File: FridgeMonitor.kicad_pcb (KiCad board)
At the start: 2 copper layers, 78 x 62 mm, 26 parts, among them J1 Conn_01x03, J2 Conn_01x03, J3 Conn_01x03, J4 Conn_01x03, J6 Conn_02x04_Odd_Even, J7 USB_B_Micro, U1 ESP-01v090, U2 LM2594M-3.3

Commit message: Backup
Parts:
- added JP1: SolderJumper_3_Bridged12, Jumper:SolderJumper-3_P1.3mm_Open_Pad1.0x1.5mm, F.Cu at (96.5, 80.0)
- added JP2: SolderJumper_3_Bridged12, Jumper:SolderJumper-3_P1.3mm_Open_Pad1.0x1.5mm, F.Cu at (77.5, 80.0)
- added JP3: SolderJumper_3_Bridged12, Jumper:SolderJumper-3_P1.3mm_Open_Pad1.0x1.5mm, F.Cu at (61.0, 80.0)
- added JP4: SolderJumper_3_Bridged12, Jumper:SolderJumper-3_P1.3mm_Open_Pad1.0x1.5mm, F.Cu at (53.3, 80.0)
- added R5: 0R, Resistor_SMD:R_0805_2012Metric_Pad1.20x1.40mm_HandSolder, F.Cu at (88.0, 51.5)
- added R6: 100k, Resistor_SMD:R_0805_2012Metric_Pad1.20x1.40mm_HandSolder, F.Cu at (88.0, 54.4)
- added REF**: MountingHole_3.2mm_M3, MountingHole:MountingHole_3.2mm_M3, F.Cu at (104.5, 86.0)
- added REF**: MountingHole_3.2mm_M3, MountingHole:MountingHole_3.2mm_M3, F.Cu at (69.0, 36.0)
- added REF**: MountingHole_3.2mm_M3, MountingHole:MountingHole_3.2mm_M3, F.Cu at (33.5, 36.0)
- added REF**: MountingHole_3.2mm_M3, MountingHole:MountingHole_3.2mm_M3, F.Cu at (33.5, 86.0)
- added REF**: MountingHole_3.2mm_M3, MountingHole:MountingHole_3.2mm_M3, F.Cu at (104.5, 36.0)
- moved D3 4.63 mm to (46.5, 39.5)
- moved R2 4.06 mm to (54.6, 74.9)
- moved R3 4.01 mm to (59.7, 75.0)
- moved C9 3.67 mm to (41.7, 39.5)
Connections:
- C1 pad 1: +3V3 -> Net-(J1-Pin_3)
- C2 pad 1: +3V3 -> Net-(J2-Pin_3)
- C3 pad 1: +3V3 -> Net-(J3-Pin_3)
- C4 pad 1: +3V3 -> Net-(J4-Pin_3)
- C5 pad 1: +3V3 -> Net-(J1-Pin_3)
- C6 pad 1: +3V3 -> Net-(J2-Pin_3)
- C7 pad 1: +3V3 -> Net-(J3-Pin_3)
- C8 pad 1: +3V3 -> Net-(J4-Pin_3)
- J1 pad 3: +3V3 -> Net-(J1-Pin_3)
- J2 pad 3: +3V3 -> Net-(J2-Pin_3)
- J3 pad 3: +3V3 -> Net-(J3-Pin_3)
- J4 pad 3: +3V3 -> Net-(J4-Pin_3)
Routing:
- net +3V3: track 163.6 -> 125.2 mm, vias 1 -> 4
- net Net-(J2-Pin_3): track 0.00 -> 20.9 mm
- net Net-(J4-Pin_3): track 0.00 -> 18.7 mm
- net Net-(J1-Pin_3): track 0.00 -> 16.4 mm
- net Net-(J3-Pin_3): track 0.00 -> 16.3 mm
- net /1-Wire: track 70.0 -> 83.6 mm
- net Net-(D3-K): track 7.97 -> 12.8 mm
- net Net-(J7-VBUS): track 20.0 -> 16.4 mm
- net Net-(J6-Pin_6): track 37.4 -> 34.1 mm

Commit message: For the moment all routed, except GND
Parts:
- added Q1: SI2301, Package_TO_SOT_SMD:TSOT-23, F.Cu at (60.7, 69.7)
- moved R6 35.1 mm to (56.4, 69.6), turned to 90 degrees
- moved R5 33.2 mm to (58.2, 66.0), turned to 180 degrees
- moved R1 3.95 mm to (41.9, 80.3), turned to -90 degrees
- moved C4 1.27 mm to (48.0, 82.5)
- moved J6 0.51 mm to (34.3, 77.0)
- moved C8 0.09 mm to (47.1, 76.2)
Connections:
- JP1 pad 3: unconnected-(JP1-B-Pad3) -> /V_sensors
- JP2 pad 3: unconnected-(JP2-B-Pad3) -> /V_sensors
- JP3 pad 3: unconnected-(JP3-B-Pad3) -> /V_sensors
- JP4 pad 3: unconnected-(JP4-B-Pad3) -> /V_sensors
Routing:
- net /V_sensors: track 0.00 -> 59.8 mm, vias 0 -> 3
- net Net-(J6-Pin_4): track 12.0 -> 47.8 mm
- net +3V3: track 125.2 -> 143.5 mm, vias 4 -> 5
- net /1-Wire: track 83.6 -> 96.4 mm
- net Net-(Q1-G): track 0.00 -> 5.87 mm
- net Net-(J4-Pin_3): track 18.7 -> 20.6 mm

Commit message: backup
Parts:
- removed the REF** at (69.0, 36.0)
- added ? (x2): , , F.Cu at (91.9, 46.5)
- added ?: , , F.Cu at (89.4, 51.6)
- added ?: , , F.Cu at (48.8, 51.6)
- added ?: , , F.Cu at (69.1, 43.9)
- added ?: , , F.Cu at (86.9, 46.5)
- added ?: , , F.Cu at (79.2, 46.5)
- added ?: , , F.Cu at (94.5, 43.9)
- added ?: , , F.Cu at (81.8, 46.5)
- added ?: , , F.Cu at (102.1, 46.5)
- added ?: , , F.Cu at (79.2, 51.6)
- added ?: , , F.Cu at (74.2, 43.9)
- added ?: , , F.Cu at (91.9, 43.9)
- added ?: , , F.Cu at (69.1, 46.5)
- added ?: , , F.Cu at (71.6, 51.6)
- added ?: , , F.Cu at (86.9, 51.6)
- added ?: , , F.Cu at (74.2, 46.5)
- added ?: , , F.Cu at (61.5, 51.6)
- added ?: , , F.Cu at (99.6, 43.9)
- added ?: , , F.Cu at (97.0, 51.6)
- added ?: , , F.Cu at (94.5, 51.6)
- added ?: , , F.Cu at (76.7, 51.6)
- added ?: , , F.Cu at (58.9, 51.6)
- added ?: , , F.Cu at (53.8, 51.6)
- added ?: , , F.Cu at (66.5, 51.6)
- added ?: , , F.Cu at (84.3, 43.9)
- added ?: , , F.Cu at (91.9, 51.6)
- added ?: , , F.Cu at (71.6, 43.9)
- added ?: , , F.Cu at (76.7, 46.5)
- added ?: , , F.Cu at (89.4, 43.9)
- added ?: , , F.Cu at (69.1, 51.6)
- added ?: , , F.Cu at (51.3, 51.6)
- added ?: , , F.Cu at (81.8, 51.6)
- added ?: , , F.Cu at (97.0, 43.9)
- added ?: , , F.Cu at (99.6, 46.5)
- added ?: , , F.Cu at (84.3, 46.5)
- added ?: , , F.Cu at (71.6, 46.5)
- added ?: , , F.Cu at (94.5, 46.5)
- added ?: , , F.Cu at (64.0, 51.6)
- added ?: , , F.Cu at (74.2, 51.6)
- added ?: , , F.Cu at (97.0, 46.5)
- added ?: , , F.Cu at (102.1, 43.9)
- added ?: , , F.Cu at (84.3, 51.6)
- added ?: , , F.Cu at (56.4, 51.6)
- added ?: , , F.Cu at (86.9, 43.9)
- added ?: , , F.Cu at (89.4, 46.5)
- added ?: , , F.Cu at (81.8, 43.9)
- added ?: , , F.Cu at (104.6, 43.9)
- added A1: RaspberryPi_Pico, OwnFootprints:EVB_PICO, F.Cu at (53.8, 66.8)
- added C13: C_Polarized, Capacitor_THT:CP_Radial_D6.3mm_P2.50mm, F.Cu at (78.9, 41.2)
- added C14: C, Capacitor_SMD:C_0805_2012Metric_Pad1.18x1.45mm_HandSolder, F.Cu at (82.9, 38.8)
- added C15: C_Polarized, Capacitor_THT:CP_Radial_D6.3mm_P2.50mm, F.Cu at (64.5, 33.8)
- added C16: C, Capacitor_SMD:C_0805_2012Metric_Pad1.18x1.45mm_HandSolder, F.Cu at (66.3, 38.6)
- added J10: Conn_01x02_Pin, Connector_PinSocket_2.54mm:PinSocket_1x02_P2.54mm_Vertical, F.Cu at (71.6, 41.4)
- added J11: Conn_01x03, Connector_Phoenix_MC_HighVoltage:PhoenixContact_MC_1,5_3-G-5.08_1x03_P5.08mm_Horizontal, F.Cu at (80.2, 35.2)
- added J5: Conn_01x03, Connector_Phoenix_MC_HighVoltage:PhoenixContact_MC_1,5_3-G-5.08_1x03_P5.08mm_Horizontal, F.Cu at (97.0, 35.3)
- added J8: Conn_01x02_Pin, Connector_PinSocket_2.54mm:PinSocket_1x02_P2.54mm_Vertical, F.Cu at (89.4, 41.4)
- added J9: Conn_01x02_Pin, Connector_PinSocket_2.54mm:PinSocket_1x02_P2.54mm_Vertical, F.Cu at (32.2, 41.5)
- moved Q1 27.3 mm to (37.7, 55.2), turned to 90 degrees
- moved R5 25.5 mm to (34.0, 57.8), turned to -90 degrees
- moved R6 21.3 mm to (37.6, 59.5), turned to 180 degrees
- moved C12 19.3 mm to (62.0, 44.7), turned to 90 degrees
- moved L1 15.0 mm to (53.5, 33.5), turned to -90 degrees
- moved D3 5.52 mm to (46.0, 45.0)
- moved R4 4.02 mm to (41.0, 52.0), turned to 180 degrees
- moved C10 3.79 mm to (45.0, 69.0), turned to -90 degrees
- moved C11 1.69 mm to (49.5, 69.0), turned to -90 degrees
- moved C8 1.33 mm to (46.8, 77.5)
- moved JP4 0.69 mm to (54.0, 80.0)
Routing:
- net +3V3: track 143.5 -> 175.3 mm, vias 5 -> 6
- net /V_sensors: track 59.8 -> 91.4 mm, vias 3 -> 4
- net Net-(J6-Pin_4): track 47.8 -> 18.3 mm
- net Net-(J5-Pin_3): track 0.00 -> 17.1 mm
- net Net-(D3-K): track 12.8 -> 22.4 mm
- net Net-(J10-Pin_2): track 0.00 -> 8.35 mm
- net Net-(J7-VBUS): track 16.4 -> 24.1 mm
- net Net-(J10-Pin_1): track 0.00 -> 7.66 mm
- net Net-(J5-Pin_2): track 0.00 -> 7.15 mm
- net Net-(J4-Pin_3): track 20.6 -> 19.7 mm
- net Net-(U2-~{ON}/OFF): track 2.66 -> 1.98 mm
- net Net-(J6-Pin_6): track 34.1 -> 33.5 mm

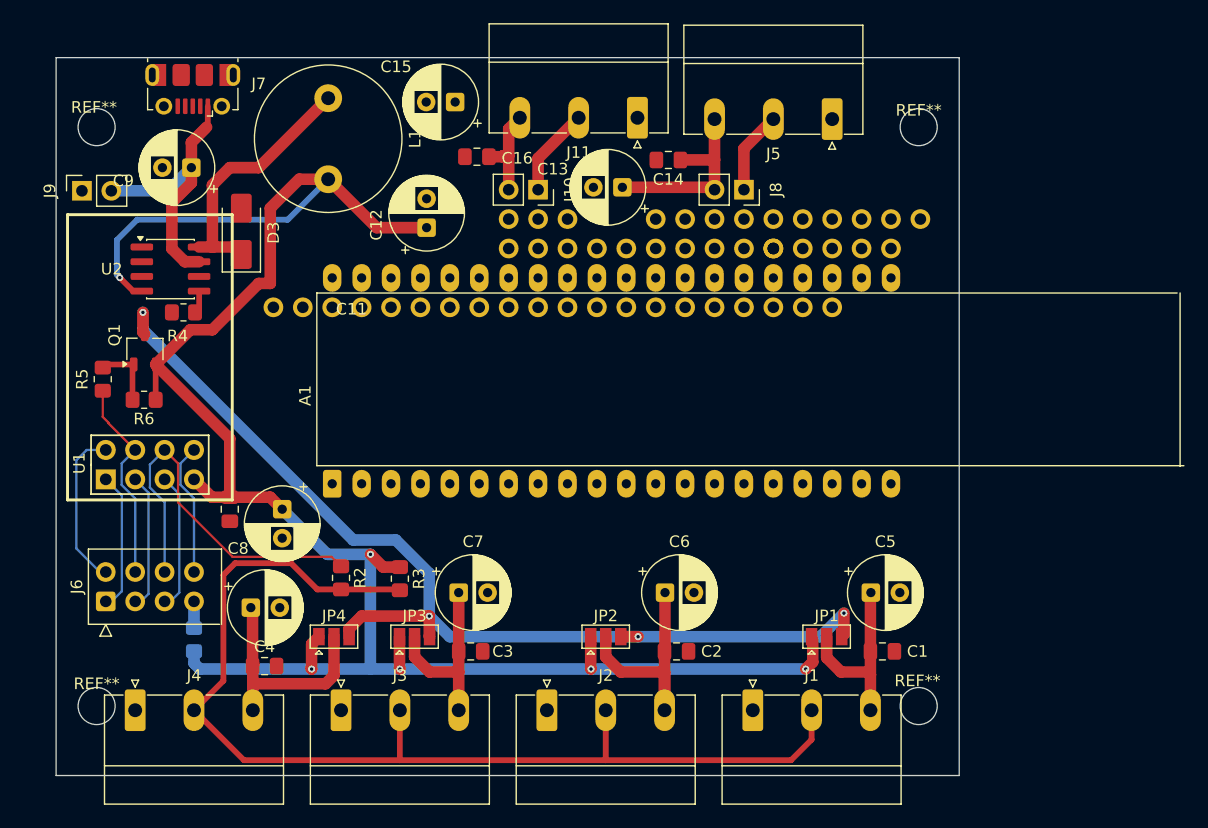
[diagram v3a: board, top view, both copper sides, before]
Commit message: all routed, except GND
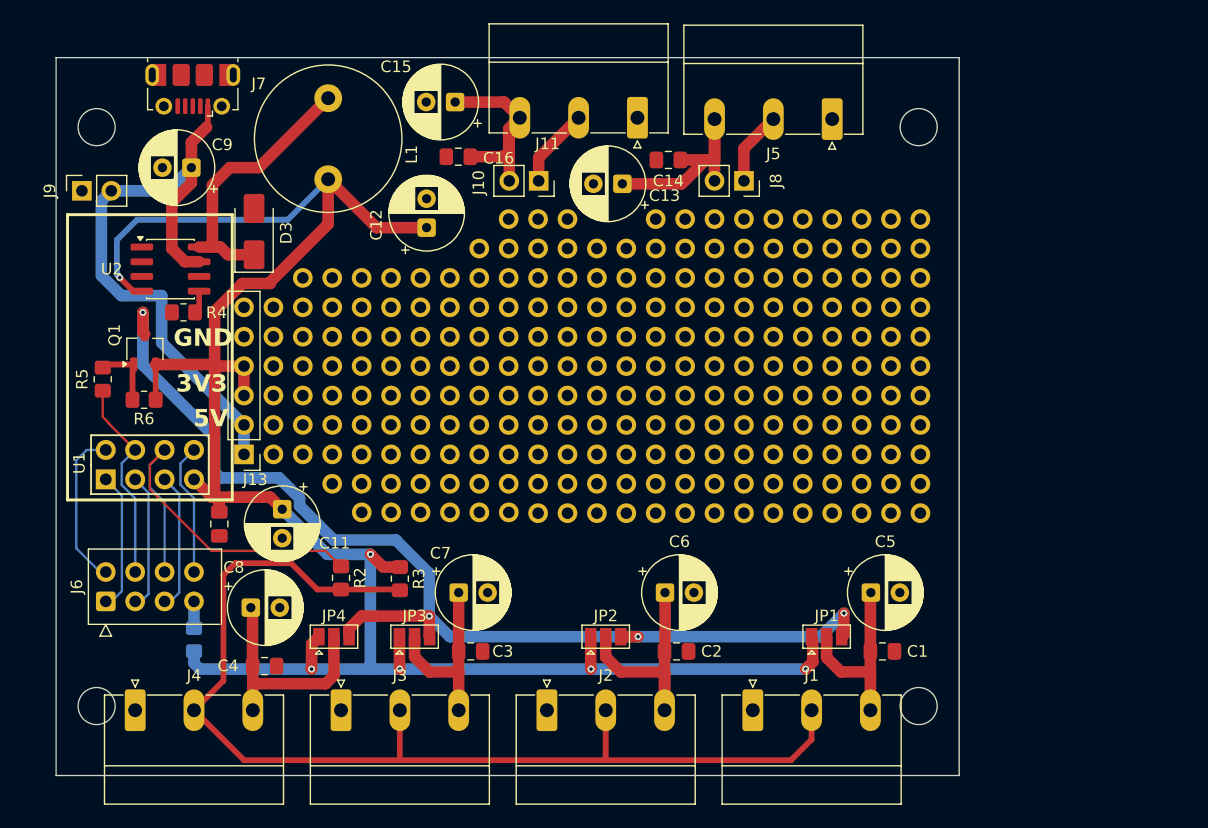
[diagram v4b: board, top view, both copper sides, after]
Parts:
- removed the ? at (91.9, 46.5)
- removed A1: RaspberryPi_Pico, OwnFootprints:EVB_PICO
- added ?: , , F.Cu at (104.6, 59.2)
- added ?: , , F.Cu at (61.5, 69.3)
- added ?: , , F.Cu at (81.8, 54.1)
- added ?: , , F.Cu at (86.9, 61.7)
- added ?: , , F.Cu at (89.4, 66.8)
- added ?: , , F.Cu at (64.0, 54.1)
- added ?: , , F.Cu at (91.9, 66.8)
- added ?: , , F.Cu at (61.5, 54.1)
- added ?: , , F.Cu at (76.7, 69.3)
- added ?: , , F.Cu at (84.3, 64.3)
- added ?: , , F.Cu at (69.1, 61.7)
- added ?: , , F.Cu at (74.2, 61.7)
- added ?: , , F.Cu at (91.9, 49.0)
- added ?: , , F.Cu at (69.1, 64.3)
- added ?: , , F.Cu at (102.1, 64.3)
- added ?: , , F.Cu at (51.3, 54.1)
- added ?: , , F.Cu at (89.4, 61.7)
- added ?: , , F.Cu at (89.4, 54.1)
- added ?: , , F.Cu at (79.2, 49.0)
- added ?: , , F.Cu at (76.7, 56.6)
- added ?: , , F.Cu at (53.8, 64.3)
- added ?: , , F.Cu at (64.0, 61.7)
- added ?: , , F.Cu at (84.3, 54.1)
- added ?: , , F.Cu at (89.4, 49.0)
- added ?: , , F.Cu at (97.0, 64.3)
- added ?: , , F.Cu at (58.9, 49.0)
- added ?: , , F.Cu at (102.1, 49.0)
- added ?: , , F.Cu at (97.0, 61.7)
- added ?: , , F.Cu at (99.6, 61.7)
- added ?: , , F.Cu at (94.5, 59.2)
- added ?: , , F.Cu at (56.4, 61.7)
- added ?: , , F.Cu at (58.9, 64.3)
- added ?: , , F.Cu at (91.9, 59.2)
- added ?: , , F.Cu at (69.1, 49.0)
- added ?: , , F.Cu at (51.3, 59.2)
- added ?: , , F.Cu at (102.1, 66.8)
- added ?: , , F.Cu at (74.2, 54.1)
- added ?: , , F.Cu at (58.9, 69.3)
- added ?: , , F.Cu at (53.8, 56.6)
- added ?: , , F.Cu at (66.5, 54.1)
- added ?: , , F.Cu at (94.5, 54.1)
- added ?: , , F.Cu at (99.6, 66.8)
- added ?: , , F.Cu at (74.2, 66.8)
- added ?: , , F.Cu at (84.3, 59.2)
- added ?: , , F.Cu at (97.0, 69.3)
- added ?: , , F.Cu at (58.9, 54.1)
- added ?: , , F.Cu at (71.6, 59.2)
- added ?: , , F.Cu at (104.6, 51.6)
- added ?: , , F.Cu at (76.7, 49.0)
- added ?: , , F.Cu at (56.4, 54.1)
- added ?: , , F.Cu at (89.4, 59.2)
- added ?: , , F.Cu at (69.1, 59.2)
- added ?: , , F.Cu at (76.7, 66.8)
- added ?: , , F.Cu at (79.2, 54.1)
- added ?: , , F.Cu at (61.5, 56.6)
- added ?: , , F.Cu at (74.2, 69.3)
- added ?: , , F.Cu at (99.6, 49.0)
- added ?: , , F.Cu at (102.1, 56.6)
- added ?: , , F.Cu at (56.4, 49.0)
- added ?: , , F.Cu at (64.0, 66.8)
- added ?: , , F.Cu at (51.3, 56.6)
- added ?: , , F.Cu at (86.9, 64.3)
- added ?: , , F.Cu at (74.2, 59.2)
- added ?: , , F.Cu at (53.8, 54.1)
- added ?: , , F.Cu at (64.0, 56.6)
- added ?: , , F.Cu at (71.6, 49.0)
- added ?: , , F.Cu at (56.4, 56.6)
- added ?: , , F.Cu at (99.6, 54.1)
- added ?: , , F.Cu at (48.8, 64.3)
- added ?: , , F.Cu at (94.5, 69.3)
- added ?: , , F.Cu at (61.5, 64.3)
- added ?: , , F.Cu at (58.9, 59.2)
- added ?: , , F.Cu at (97.0, 59.2)
- added ?: , , F.Cu at (71.6, 56.6)
- added ?: , , F.Cu at (89.4, 69.3)
- added ?: , , F.Cu at (66.5, 56.6)
- added ?: , , F.Cu at (81.8, 66.8)
- added ?: , , F.Cu at (71.6, 61.7)
- added ?: , , F.Cu at (86.9, 54.1)
- added ?: , , F.Cu at (53.8, 66.8)
- added ?: , , F.Cu at (104.6, 66.8)
- added ?: , , F.Cu at (94.5, 61.7)
- added ?: , , F.Cu at (102.1, 69.3)
- added ?: , , F.Cu at (104.6, 61.7)
- added ?: , , F.Cu at (51.3, 64.3)
- added ?: , , F.Cu at (97.0, 54.1)
- added ?: , , F.Cu at (97.0, 49.0)
- added ?: , , F.Cu at (66.5, 66.8)
- added ?: , , F.Cu at (56.4, 59.2)
- added ?: , , F.Cu at (91.9, 69.3)
- added ?: , , F.Cu at (79.2, 64.3)
- added ?: , , F.Cu at (86.9, 66.8)
- added ?: , , F.Cu at (53.8, 61.7)
- added ?: , , F.Cu at (61.5, 66.8)
- added ?: , , F.Cu at (71.6, 66.8)
- added ?: , , F.Cu at (94.5, 49.0)
- added ?: , , F.Cu at (99.6, 69.3)
- added ?: , , F.Cu at (104.6, 46.5)
- added ?: , , F.Cu at (102.1, 61.7)
- added ?: , , F.Cu at (79.2, 69.3)
- added ?: , , F.Cu at (71.6, 54.1)
- added ?: , , F.Cu at (91.9, 54.1)
- added ?: , , F.Cu at (86.9, 49.0)
- added ?: , , F.Cu at (66.5, 49.0)
- added ?: , , F.Cu at (94.5, 64.3)
- added ?: , , F.Cu at (51.3, 61.7)
- added ?: , , F.Cu at (48.8, 59.2)
- added ?: , , F.Cu at (104.6, 56.6)
- added ?: , , F.Cu at (66.6, 69.3)
- added ?: , , F.Cu at (84.3, 49.0)
- added ?: , , F.Cu at (94.5, 66.8)
- added ?: , , F.Cu at (58.9, 56.6)
- added ?: , , F.Cu at (99.6, 51.6)
- added ?: , , F.Cu at (97.0, 56.6)
- added ?: , , F.Cu at (64.0, 59.2)
- added ?: , , F.Cu at (104.6, 54.1)
- added ?: , , F.Cu at (48.8, 61.7)
- added ?: , , F.Cu at (58.9, 61.7)
- added ?: , , F.Cu at (56.4, 69.3)
- added ?: , , F.Cu at (79.2, 61.7)
- added ?: , , F.Cu at (56.4, 64.3)
- added ?: , , F.Cu at (51.3, 49.0)
- added ?: , , F.Cu at (81.8, 64.3)
- added ?: , , F.Cu at (71.6, 64.3)
- added ?: , , F.Cu at (76.7, 64.3)
- added ?: , , F.Cu at (76.7, 61.7)
- added ?: , , F.Cu at (74.2, 56.6)
- added ?: , , F.Cu at (71.6, 69.3)
- added ?: , , F.Cu at (102.1, 59.2)
- added ?: , , F.Cu at (81.8, 69.3)
- added ?: , , F.Cu at (104.6, 49.0)
- added ?: , , F.Cu at (84.3, 61.7)
- added ?: , , F.Cu at (86.9, 56.6)
- added ?: , , F.Cu at (66.5, 59.2)
- added ?: , , F.Cu at (102.1, 54.1)
- added ?: , , F.Cu at (58.9, 66.8)
- added ?: , , F.Cu at (53.8, 49.0)
- added ?: , , F.Cu at (91.9, 64.3)
- added ?: , , F.Cu at (74.2, 49.0)
- added ?: , , F.Cu at (64.0, 49.0)
- added ?: , , F.Cu at (81.8, 59.2)
- added ?: , , F.Cu at (64.0, 69.3)
- added ?: , , F.Cu at (89.4, 64.3)
- added ?: , , F.Cu at (91.9, 56.6)
- added ?: , , F.Cu at (74.2, 64.3)
- added ?: , , F.Cu at (66.5, 46.5)
- added ?: , , F.Cu at (91.9, 61.7)
- added ?: , , F.Cu at (48.8, 56.6)
- added ?: , , F.Cu at (86.9, 59.2)
- added ?: , , F.Cu at (79.2, 56.6)
- added ?: , , F.Cu at (97.0, 66.8)
- added ?: , , F.Cu at (81.8, 56.6)
- added ?: , , F.Cu at (79.2, 59.2)
- added ?: , , F.Cu at (76.7, 54.1)
- added ?: , , F.Cu at (66.5, 61.7)
- added ?: , , F.Cu at (66.5, 64.3)
- added ?: , , F.Cu at (79.2, 66.8)
- added ?: , , F.Cu at (94.5, 56.6)
- added ?: , , F.Cu at (53.8, 59.2)
- added ?: , , F.Cu at (89.4, 56.6)
- added ?: , , F.Cu at (104.6, 69.3)
- added ?: , , F.Cu at (76.7, 59.2)
- added ?: , , F.Cu at (61.5, 49.0)
- added ?: , , F.Cu at (61.5, 59.2)
- added ?: , , F.Cu at (69.1, 66.8)
- added ?: , , F.Cu at (48.8, 54.1)
- added ?: , , F.Cu at (84.3, 69.3)
- added ?: , , F.Cu at (104.6, 64.3)
- added ?: , , F.Cu at (81.8, 61.7)
- added ?: , , F.Cu at (81.8, 49.0)
- added ?: , , F.Cu at (69.1, 54.1)
- added ?: , , F.Cu at (61.5, 61.7)
- added ?: , , F.Cu at (84.3, 66.8)
- added ?: , , F.Cu at (99.6, 56.6)
- added ?: , , F.Cu at (86.9, 69.3)
- added ?: , , F.Cu at (69.1, 56.6)
- added ?: , , F.Cu at (99.6, 59.2)
- added ?: , , F.Cu at (56.4, 66.8)
- added ?: , , F.Cu at (64.0, 64.3)
- added ?: , , F.Cu at (84.3, 56.6)
- added ?: , , F.Cu at (69.1, 69.3)
- added ?: , , F.Cu at (102.1, 51.6)
- added ?: , , F.Cu at (99.6, 64.3)
- added J13: Conn_01x06_Pin, Connector_PinHeader_2.54mm:PinHeader_1x06_P2.54mm_Vertical, F.Cu at (46.2, 64.3)
- moved C16 1.60 mm to (64.7, 38.6)
- moved C10 1.56 mm to (44.1, 70.3)
- moved D3 1.10 mm to (47.1, 45.0)
- moved J10 0.76 mm to (71.7, 40.6)
- moved J8 0.76 mm to (89.4, 40.6)
- moved C13 0.30 mm to (78.9, 40.9)
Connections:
- net Net-(J7-VBUS) renamed +5V
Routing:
- net +5V: track 24.1 -> 54.4 mm
- net Net-(J10-Pin_2): track 8.35 -> 19.1 mm
- net +3V3: track 175.3 -> 180.7 mm
- net /V_sensors: track 91.4 -> 95.4 mm
- net Net-(J5-Pin_3): track 17.1 -> 19.9 mm
- net Net-(J6-Pin_6): track 33.5 -> 35.3 mm
- net Net-(D3-K): track 22.4 -> 23.5 mm
- net Net-(J10-Pin_1): track 7.66 -> 6.88 mm
- net Net-(J5-Pin_2): track 7.15 -> 6.39 mm
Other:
- board text added: "3V3"
- board text added: "5V"
- board text added: "GND"

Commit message: GND plane, DRC ok
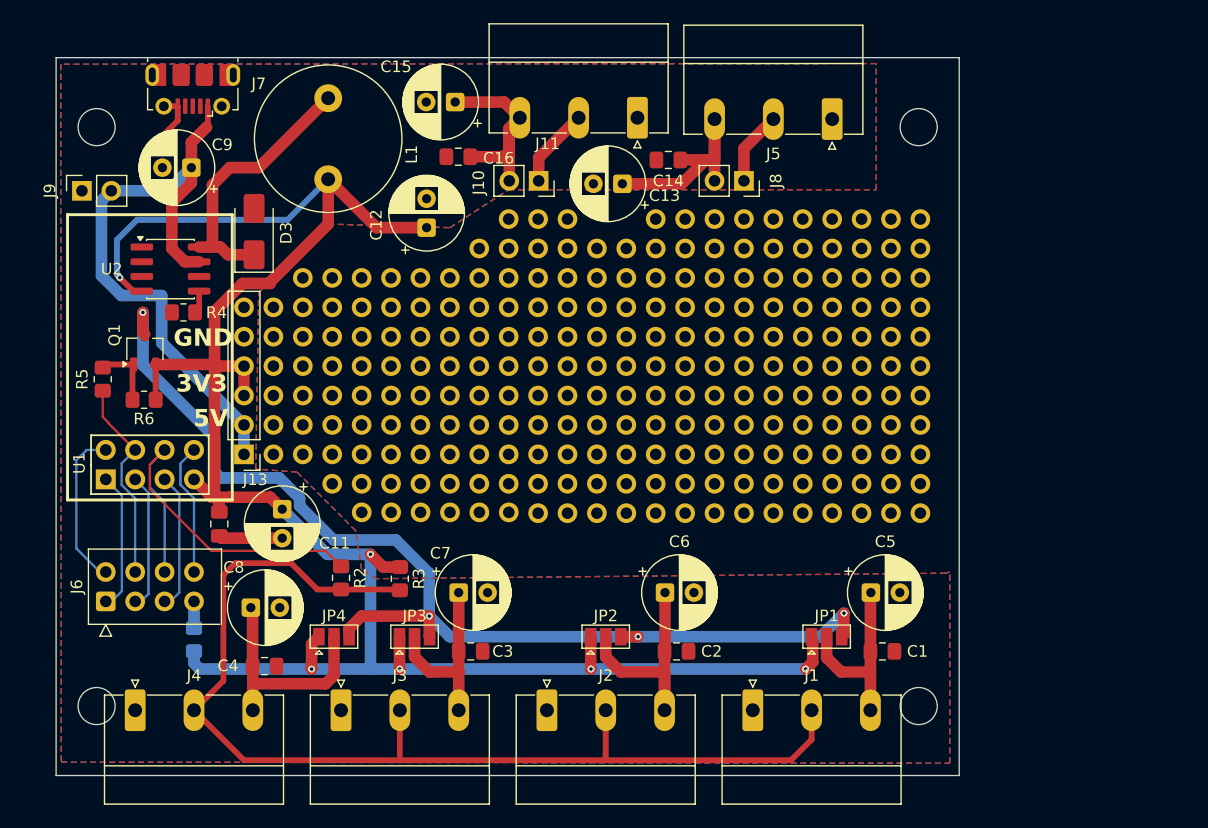
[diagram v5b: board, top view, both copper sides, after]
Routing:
- net GND: track 0.00 -> 9.92 mm
- added copper zone on B.Cu, net GND
- added copper zone on F.Cu, net GND
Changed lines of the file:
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@@
+	)
+	(segment
+		(start 40.504 34.196)
+		(end 40.504 35.442)
+		(width 0.5)
+		(layer "F.Cu")
+		(net "GND")
+	)
+	(segment
+		(start 40.504 35.442)
+		(end 39.116 36.83)
+		(width 0.5)
+		(layer "F.Cu")
+		(net "GND")
+	)
+	(segment
+		(start 49.53 71.5)
+		(end 44.2885 71.5)
+		(width 1)
+		(layer "F.Cu")
+		(net "GND")
+	)
+	(segment
+		(start 44.2885 71.5)
+		(end 44.098 71.3095)
+		(width 1)
+		(layer "F.Cu")
+		(net "GND")
+	)
+	(segment
+		(start 40.504 34.196)
+		(end 39.304 34.196)
+		(width 0.5)
+		(layer "F.Cu")
+		(net "GND")
 	)
 	(segment
@@
 		(net "Net-(J6-Pin_4)")
 	)
+	(zone
+		(net "GND")
+		(layers "F.Cu" "B.Cu")
+		(hatch edge 0.5)
+		(connect_pads
+			(clearance 0.5)
+		)
+		(min_thickness 0.25)
+		(fill yes
+			(thermal_gap 0.5)
+			(thermal_bridge_width 0.5)
+			(island_removal_mode 0)
+		)
+		(polygon
+			(pts
+				(xy 106.848 74.522) (xy 57.658004 75) (xy 56.388 74.209775) (xy 55.88 70.866) (xy 50.8 65.786) (xy 47.244 65.532)
+				(xy 47.498 50.292) (xy 53.5 44.37) (xy 64.008 44.68238) (xy 69.088 41.402) (xy 100.838 41.402) (xy 100.838 30.514921)
+				(xy 30.405415 30.560927) (xy 30.444789 90.840792) (xy 107.188 90.932) (xy 107.188 74.422)
+			)
+		)
+	)
 	(embedded_fonts no)
